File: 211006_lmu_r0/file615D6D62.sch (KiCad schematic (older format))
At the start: 23 parts, among them U1 R-78C5.0-1.0

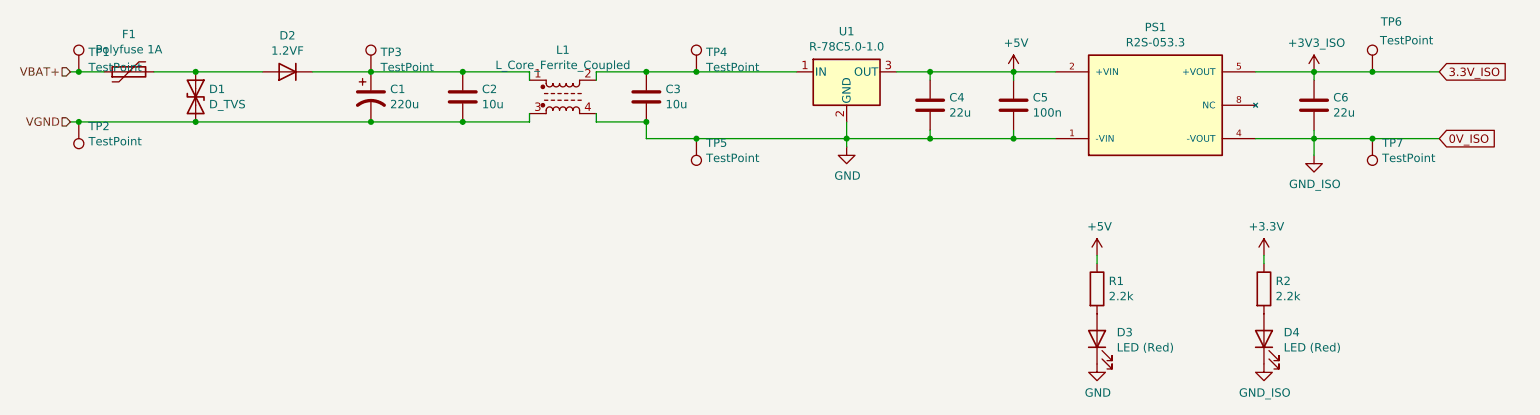
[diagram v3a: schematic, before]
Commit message: Updated with Mouser links for BOM
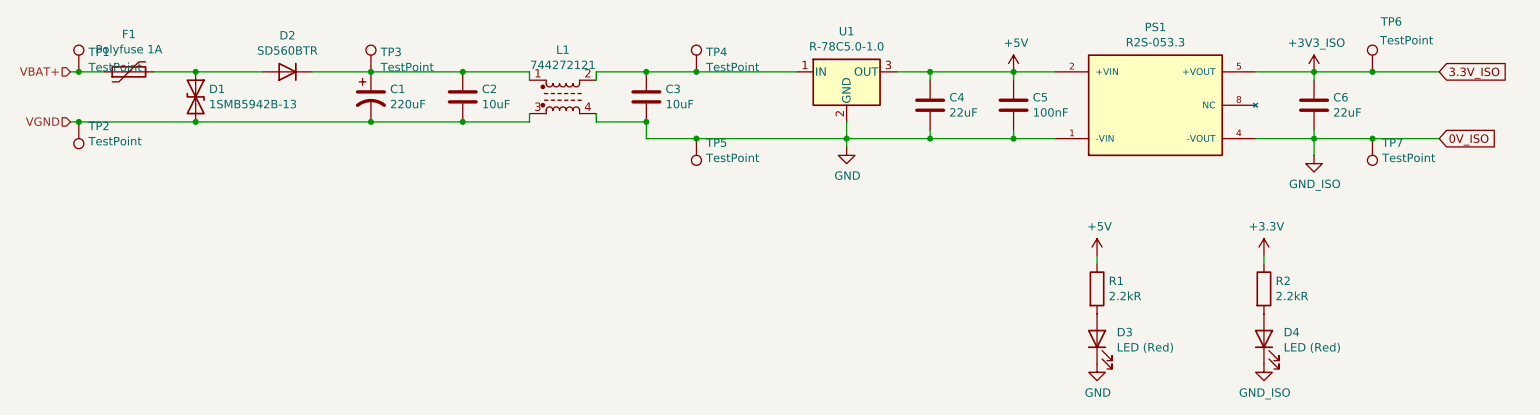
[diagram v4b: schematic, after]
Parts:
- C1: value 220u -> 220uF; Manufacturer (none) -> Vishay; Mouser Part Number (none) -> 594-MAL214699106E3; Mouser URL (none) -> https://au.mouser.com/ProductDetail/Vishay-BC-Components/MA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
- C2, C3: value 10u -> 10uF
- C4, C6: value 22u -> 22uF
- C5: value 100n -> 100nF
- D1: value D_TVS -> 1SMB5942B-13; Mouser Part Number (none) -> 621-1SMB5942B-13; Mouser URL (none) -> https://au.mouser.com/ProductDetail/Diodes-Incorporated/1SM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
- D2: value 1.2VF -> SD560BTR; Mouser Part Number (none) -> NOT AVAILABLE!; Mouser URL (none) -> NOT AVAILABLE!
- D3, D4: Manufacturer (none) -> AMS OSRAM; Mouser Part Number (none) -> 720-LSR976-NR-1; Mouser URL (none) -> https://au.mouser.com/ProductDetail/ams-OSRAM/LS-R976-NR-1-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; Part Number (none) -> LS R976-NR-1-0-20-R18
- F1: Mouser Part Number (none) -> 530-0ZCF0100AF2A; Mouser URL (none) -> https://au.mouser.com/ProductDetail/Bel-Fuse/0ZCF0100AF2A?q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
- L1: value L_Core_Ferrite_Coupled -> 744272121; Manufacturer (none) -> Wurth; Mouser Part Number (none) -> 710-744272121; Mouser URL (none) -> https://au.mouser.com/ProductDetail/Wurth-Elektronik/744272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
- PS1: MANUFACTURER RECOM -> (none); Manufacturer (none) -> RECOM; Mouser Part Number (none) -> 919-R2S-053.3; Mouser URL (none) -> https://au.mouser.com/ProductDetail/RECOM-Power/R2S-0533?qs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; Part Number (none) -> 919-R2S-053.3; STANDARD Manufacturer Recommendations -> (none)
- R1, R2: value 2.2k -> 2.2kR
- TP1, TP2, TP3, TP4, TP5, TP6, TP7: Manufacturer (none) -> -; Mouser Part Number (none) -> -; Mouser URL (none) -> -; Part Number (none) -> -
- U1: Manufacturer (none) -> RECOM; Mouser Part Number (none) -> 919-R-78C5.0-1.0; Mouser URL (none) -> https://au.mouser.com/ProductDetail/RECOM-Power/R-78C50-10?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; Part Number (none) -> R-78C5.0-1.0
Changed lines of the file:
@@
 F 2 "Converter_DCDC:Converter_DCDC_RECOM_R-78E-0.5_THT" H 6600 2100 50  0001 L CIN
 F 3 "https://www.recom-power.com/pdf/Innoline/R-78Cxx-1.0.pdf" H 6550 2350 50  0001 C CNN
+F 4 "R-78C5.0-1.0" H 6550 2350 50  0001 C CNN "Part Number"
+F 5 "RECOM" H 6550 2350 50  0001 C CNN "Manufacturer"
+F 6 "919-R-78C5.0-1.0" H 6550 2350 50  0001 C CNN "Mouser Part Number"
+F 7 "https://au.mouser.com/ProductDetail/RECOM-Power/R-78C50-10?qs=sGAEpiMZZMs7Ab1RACNF3AuU4LGLjBGD4EiimKouwhs%3D" H 6550 2350 50  0001 C CNN "Mouser URL"
 	1    6550 2350
 	1    0    0    -1
@@
 F 2 "CONV_R2S-053.3" H 8400 2550 50  0001 L BNN
 F 3 "" H 8400 2550 50  0001 L BNN
-F 4 "RECOM" H 8400 2550 50  0001 L BNN "MANUFACTURER"
+F 4 "" H 8400 2550 50  0001 L BNN "MANUFACTURER"
 F 5 "9.0mm" H 8400 2550 50  0001 L BNN "MAXIMUM_PACKAGE_HEIGHT"
-F 6 "Manufacturer Recommendations" H 8400 2550 50  0001 L BNN "STANDARD"
+F 6 "" H 8400 2550 50  0001 L BNN "STANDARD"
 F 7 "0" H 8400 2550 50  0001 L BNN "PARTREV"
+F 8 "RECOM" H 8400 2550 50  0001 C CNN "Manufacturer"
+F 9 "919-R2S-053.3" H 8400 2550 50  0001 C CNN "Mouser Part Number"
+F 10 "https://au.mouser.com/ProductDetail/RECOM-Power/R2S-0533?qs=XF8hdbuHJAU8%2FoDdSFUU9w%3D%3D" H 8400 2550 50  0001 C CNN "Mouser URL"
+F 11 "919-R2S-053.3" H 8400 2550 50  0001 C CNN "Part Number"
 	1    8400 2550
 	1    0    0    -1
@@
 P 4850 2500
 F 0 "L1" H 4850 2781 50  0000 C CNN
-F 1 "L_Core_Ferrite_Coupled" H 4850 2690 50  0000 C CNN
+F 1 "744272121" H 4850 2690 50  0000 C CNN
 F 2 "Inductor_SMD:L_CommonModeChoke_Wuerth_WE-SL5" H 4850 2500 50  0001 C CNN
 F 3 "~" H 4850 2500 50  0001 C CNN
 F 4 "744272121" H 4850 2500 50  0001 C CNN "Part Number"
+F 5 "Wurth" H 4850 2500 50  0001 C CNN "Manufacturer"
+F 6 "710-744272121" H 4850 2500 50  0001 C CNN "Mouser Part Number"
+F 7 "https://au.mouser.com/ProductDetail/Wurth-Elektronik/744272121?qs=PGXP4M47uW7bXHmb3ZYlsQ%3D%3D" H 4850 2500 50  0001 C CNN "Mouser URL"
 	1    4850 2500
 	1    0    0    -1
@@
 P 9350 2550
 F 0 "C6" H 9465 2596 50  0000 L CNN
-F 1 "22u" H 9465 2505 50  0000 L CNN
+F 1 "22uF" H 9465 2505 50  0000 L CNN
 F 2 "Capacitor_SMD:C_0805_2012Metric_Pad1.18x1.45mm_HandSolder" H 9388 2400 50  0001 C CNN
 F 3 "~" H 9350 2550 50  0001 C CNN
@@
 P 7050 2550
 F 0 "C4" H 7165 2596 50  0000 L CNN
-F 1 "22u" H 7165 2505 50  0000 L CNN
+F 1 "22uF" H 7165 2505 50  0000 L CNN
 F 2 "Capacitor_SMD:C_0805_2012Metric_Pad1.18x1.45mm_HandSolder" H 7088 2400 50  0001 C CNN
 F 3 "~" H 7050 2550 50  0001 C CNN
@@
 P 7550 2550
 F 0 "C5" H 7665 2596 50  0000 L CNN
-F 1 "100n" H 7665 2505 50  0000 L CNN
+F 1 "100nF" H 7665 2505 50  0000 L CNN
 F 2 "Capacitor_SMD:C_0603_1608Metric_Pad1.08x0.95mm_HandSolder" H 7588 2400 50  0001 C CNN
 F 3 "~" H 7550 2550 50  0001 C CNN
@@
 P 4250 2500
 F 0 "C2" H 4365 2546 50  0000 L CNN
-F 1 "10u" H 4365 2455 50  0000 L CNN
+F 1 "10uF" H 4365 2455 50  0000 L CNN
 F 2 "Capacitor_SMD:C_0805_2012Metric_Pad1.18x1.45mm_HandSolder" H 4288 2350 50  0001 C CNN
 F 3 "~" H 4250 2500 50  0001 C CNN
@@
 P 3700 2500
 F 0 "C1" H 3815 2546 50  0000 L CNN
-F 1 "220u" H 3815 2455 50  0000 L CNN
+F 1 "220uF" H 3815 2455 50  0000 L CNN
 F 2 "Capacitor_SMD:CP_Elec_10x12.5" H 3700 2500 50  0001 C CNN
 F 3 "~" H 3700 2500 50  0001 C CNN
 F 4 "MAL214699106E3" H 3700 2500 50  0001 C CNN "Part Number"
+F 5 "Vishay" H 3700 2500 50  0001 C CNN "Manufacturer"
+F 6 "594-MAL214699106E3" H 3700 2500 50  0001 C CNN "Mouser Part Number"
+F 7 "https://au.mouser.com/ProductDetail/Vishay-BC-Components/MAL214699106E3?qs=sGAEpiMZZMtZ661ya8CuXbh6ajJyr6ISA0VT%252B8eqkqw%3D" H 3700 2500 50  0001 C CNN "Mouser URL"
 	1    3700 2500
 	1    0    0    -1
@@
 P 5350 2500
 F 0 "C3" H 5465 2546 50  0000 L CNN
-F 1 "10u" H 5465 2455 50  0000 L CNN
+F 1 "10uF" H 5465 2455 50  0000 L CNN
 F 2 "Capacitor_SMD:C_0805_2012Metric_Pad1.18x1.45mm_HandSolder" H 5388 2350 50  0001 C CNN
 F 3 "~" H 5350 2500 50  0001 C CNN
@@
 P 2650 2500
 F 0 "D1" V 2604 2580 50  0000 L CNN
-F 1 "D_TVS" V 2695 2580 50  0000 L CNN
+F 1 "1SMB5942B-13" V 2695 2580 50  0000 L CNN
 F 2 "Diode_SMD:D_SMB_Handsoldering" H 2650 2500 50  0001 C CNN
 F 3 "~" H 2650 2500 50  0001 C CNN
 F 4 "1SMB5942B-13" V 2650 2500 50  0001 C CNN "Part Number"
 F 5 "Diodes Inc" V 2650 2500 50  0001 C CNN "Manufacturer"
+F 6 "621-1SMB5942B-13" H 2650 2500 50  0001 C CNN "Mouser Part Number"
+F 7 "https://au.mouser.com/ProductDetail/Diodes-Incorporated/1SMB5942B-13?qs=uwKJARvjadMY8LI4ZfMqKA%3D%3D" H 2650 2500 50  0001 C CNN "Mouser URL"
 	1    2650 2500
 	0    1    1    0
@@
 P 3200 2350
 F 0 "D2" H 3200 2133 50  0000 C CNN
-F 1 "1.2VF" H 3200 2224 50  0000 C CNN
+F 1 "SD560BTR" H 3200 2224 50  0000 C CNN
 F 2 "Diode_SMD:D_SMB_Handsoldering" H 3200 2350 50  0001 C CNN
 F 3 "~" H 3200 2350 50  0001 C CNN
 F 4 "SD560BTR" H 3200 2350 50  0001 C CNN "Part Number"
 F 5 "SMC Diode Solutions" H 3200 2350 50  0001 C CNN "Manufacturer"
+F 6 "NOT AVAILABLE!" H 3200 2350 50  0001 C CNN "Mouser Part Number"
+F 7 "NOT AVAILABLE!" H 3200 2350 50  0001 C CNN "Mouser URL"
 	1    3200 2350
 	-1   0    0    1
@@
 F 4 "0ZCF0100AF2A" V 2250 2350 50  0001 C CNN "Part Number"
 F 5 "Littelfuse" V 2250 2350 50  0001 C CNN "Manufacturer"
+F 6 "530-0ZCF0100AF2A" H 2250 2350 50  0001 C CNN "Mouser Part Number"
+F 7 "https://au.mouser.com/ProductDetail/Bel-Fuse/0ZCF0100AF2A?qs=sGAEpiMZZMvShe%252BZiYheisCiVCQm%2FacC38BFZwxSYiI%3D" H 2250 2350 50  0001 C CNN "Mouser URL"
 	1    2250 2350
 	0    -1   -1   0
@@
 P 9050 3650
 F 0 "R2" H 9120 3696 50  0000 L CNN
-F 1 "2.2k" H 9120 3605 50  0000 L CNN
+F 1 "2.2kR" H 9120 3605 50  0000 L CNN
 F 2 "Resistor_SMD:R_0603_1608Metric_Pad0.98x0.95mm_HandSolder" V 8980 3650 50  0001 C CNN
 F 3 "~" H 9050 3650 50  0001 C CNN
@@
 P 8050 3650
 F 0 "R1" H 8120 3696 50  0000 L CNN
-F 1 "2.2k" H 8120 3605 50  0000 L CNN
+F 1 "2.2kR" H 8120 3605 50  0000 L CNN
 F 2 "Resistor_SMD:R_0603_1608Metric_Pad0.98x0.95mm_HandSolder" V 7980 3650 50  0001 C CNN
 F 3 "~" H 8050 3650 50  0001 C CNN
@@
 F 2 "LED_SMD:LED_0805_2012Metric_Pad1.15x1.40mm_HandSolder" H 8050 3950 50  0001 C CNN
 F 3 "~" H 8050 3950 50  0001 C CNN
+F 4 "AMS OSRAM" H 8050 3950 50  0001 C CNN "Manufacturer"
+F 5 "720-LSR976-NR-1" H 8050 3950 50  0001 C CNN "Mouser Part Number"
+F 6 "https://au.mouser.com/ProductDetail/ams-OSRAM/LS-R976-NR-1-0-20-R18?qs=sGAEpiMZZMt82OzCyDsLFGbrp1fQkD8H8bij58Oys9s%3D" H 8050 3950 50  0001 C CNN "Mouser URL"
+F 7 "LS R976-NR-1-0-20-R18" H 8050 3950 50  0001 C CNN "Part Number"
 	1    8050 3950
 	0    -1   -1   0
@@
 F 2 "TestPoint:TestPoint_Pad_D1.0mm" H 5850 2350 50  0001 C CNN
 F 3 "~" H 5850 2350 50  0001 C CNN
+F 4 "-" H 5650 2350 50  0001 C CNN "Part Number"
+F 5 "-" H 5650 2350 50  0001 C CNN "Manufacturer"
+F 6 "-" H 5650 2350 50  0001 C CNN "Mouser Part Number"
+F 7 "-" H 5650 2350 50  0001 C CNN "Mouser URL"
 	1    5650 2350
 	1    0    0    -1
@@
 F 2 "TestPoint:TestPoint_Pad_D1.0mm" H 3900 2350 50  0001 C CNN
 F 3 "~" H 3900 2350 50  0001 C CNN
+F 4 "-" H 3700 2350 50  0001 C CNN "Part Number"
+F 5 "-" H 3700 2350 50  0001 C CNN "Manufacturer"
+F 6 "-" H 3700 2350 50  0001 C CNN "Mouser Part Number"
+F 7 "-" H 3700 2350 50  0001 C CNN "Mouser URL"
 	1    3700 2350
 	1    0    0    -1
@@
 F 2 "TestPoint:TestPoint_Pad_D1.0mm" H 2150 2350 50  0001 C CNN
 F 3 "~" H 2150 2350 50  0001 C CNN
+F 4 "-" H 1950 2350 50  0001 C CNN "Part Number"
+F 5 "-" H 1950 2350 50  0001 C CNN "Manufacturer"
+F 6 "-" H 1950 2350 50  0001 C CNN "Mouser Part Number"
+F 7 "-" H 1950 2350 50  0001 C CNN "Mouser URL"
 	1    1950 2350
 	1    0    0    -1
@@
 F 2 "TestPoint:TestPoint_Pad_D1.0mm" H 2150 2650 50  0001 C CNN
 F 3 "~" H 2150 2650 50  0001 C CNN
+F 4 "-" H 1950 2650 50  0001 C CNN "Part Number"
+F 5 "-" H 1950 2650 50  0001 C CNN "Manufacturer"
+F 6 "-" H 1950 2650 50  0001 C CNN "Mouser Part Number"
+F 7 "-" H 1950 2650 50  0001 C CNN "Mouser URL"
 	1    1950 2650
 	-1   0    0    1
@@
 F 2 "TestPoint:TestPoint_Pad_D1.0mm" H 5850 2750 50  0001 C CNN
 F 3 "~" H 5850 2750 50  0001 C CNN
+F 4 "-" H 5650 2750 50  0001 C CNN "Part Number"
+F 5 "-" H 5650 2750 50  0001 C CNN "Manufacturer"
+F 6 "-" H 5650 2750 50  0001 C CNN "Mouser Part Number"
+F 7 "-" H 5650 2750 50  0001 C CNN "Mouser URL"
 	1    5650 2750
 	-1   0    0    1
@@
 F 2 "TestPoint:TestPoint_Pad_D1.0mm" H 9900 2350 50  0001 C CNN
 F 3 "~" H 9900 2350 50  0001 C CNN
+F 4 "-" H 9700 2350 50  0001 C CNN "Part Number"
+F 5 "-" H 9700 2350 50  0001 C CNN "Manufacturer"
+F 6 "-" H 9700 2350 50  0001 C CNN "Mouser Part Number"
+F 7 "-" H 9700 2350 50  0001 C CNN "Mouser URL"
 	1    9700 2350
 	1    0    0    -1
@@
 F 2 "TestPoint:TestPoint_Pad_D1.0mm" H 9900 2750 50  0001 C CNN
 F 3 "~" H 9900 2750 50  0001 C CNN
+F 4 "-" H 9700 2750 50  0001 C CNN "Part Number"
+F 5 "-" H 9700 2750 50  0001 C CNN "Manufacturer"
+F 6 "-" H 9700 2750 50  0001 C CNN "Mouser Part Number"
+F 7 "-" H 9700 2750 50  0001 C CNN "Mouser URL"
 	1    9700 2750
 	-1   0    0    1
@@
 F 2 "LED_SMD:LED_0805_2012Metric_Pad1.15x1.40mm_HandSolder" H 9050 3950 50  0001 C CNN
 F 3 "~" H 9050 3950 50  0001 C CNN
+F 4 "AMS OSRAM" H 9050 3950 50  0001 C CNN "Manufacturer"
+F 5 "720-LSR976-NR-1" H 9050 3950 50  0001 C CNN "Mouser Part Number"
+F 6 "https://au.mouser.com/ProductDetail/ams-OSRAM/LS-R976-NR-1-0-20-R18?qs=sGAEpiMZZMt82OzCyDsLFGbrp1fQkD8H8bij58Oys9s%3D" H 9050 3950 50  0001 C CNN "Mouser URL"
+F 7 "LS R976-NR-1-0-20-R18" H 9050 3950 50  0001 C CNN "Part Number"
 	1    9050 3950
 	0    -1   -1   0
